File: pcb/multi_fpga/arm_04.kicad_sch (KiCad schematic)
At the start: 16 parts, among them U33 IM72D128V01XTMA1, U34 IM72D128V01XTMA1, U35 IM72D128V01XTMA1, U36 IM72D128V01XTMA1, U37 IM72D128V01XTMA1, U38 IM72D128V01XTMA1, U39 IM72D128V01XTMA1, U40 IM72D128V01XTMA1

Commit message: Fixed library and power issues.
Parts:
- C33, C34, C35, C36, C37, C38, C39, C40: symbol C -> multi_fpga:C
- U33, U34, U35, U36, U37, U38, U39, U40: symbol IM72D128 -> multi_fpga:IM72D128

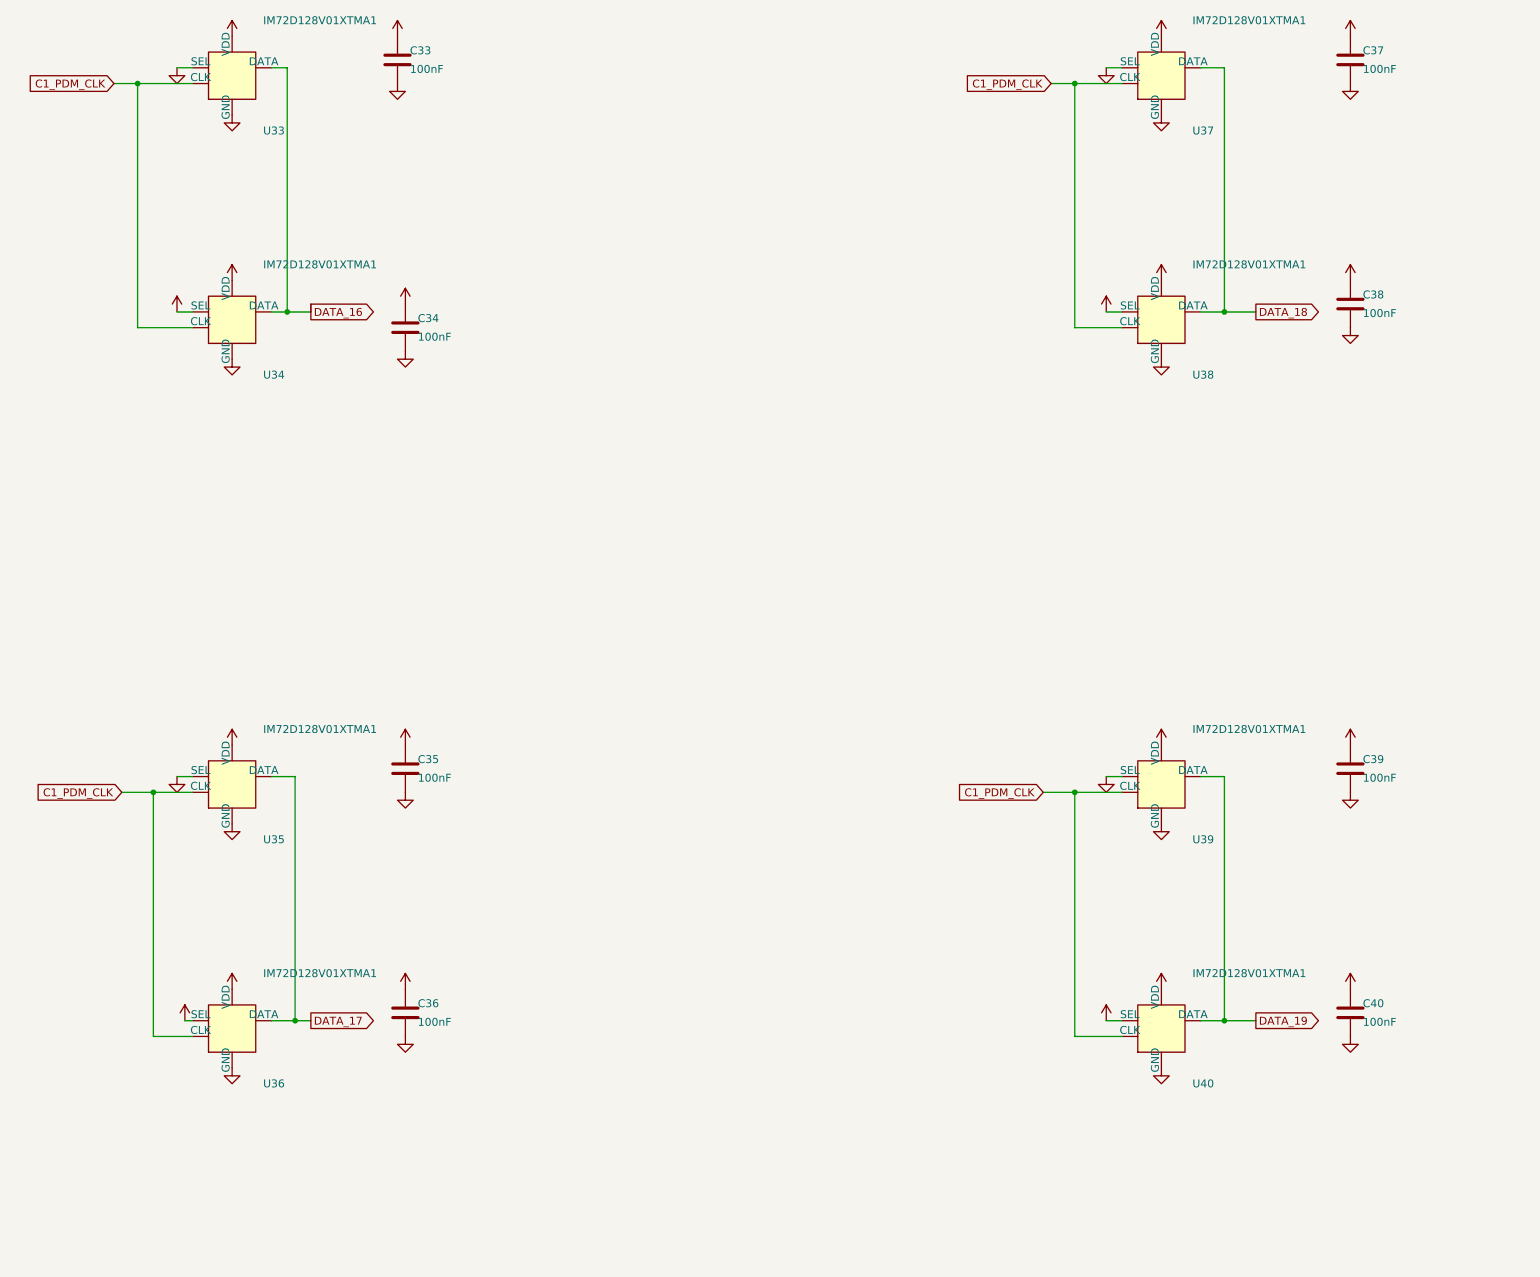
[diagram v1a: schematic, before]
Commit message: Fixed power and C ref des collisions.
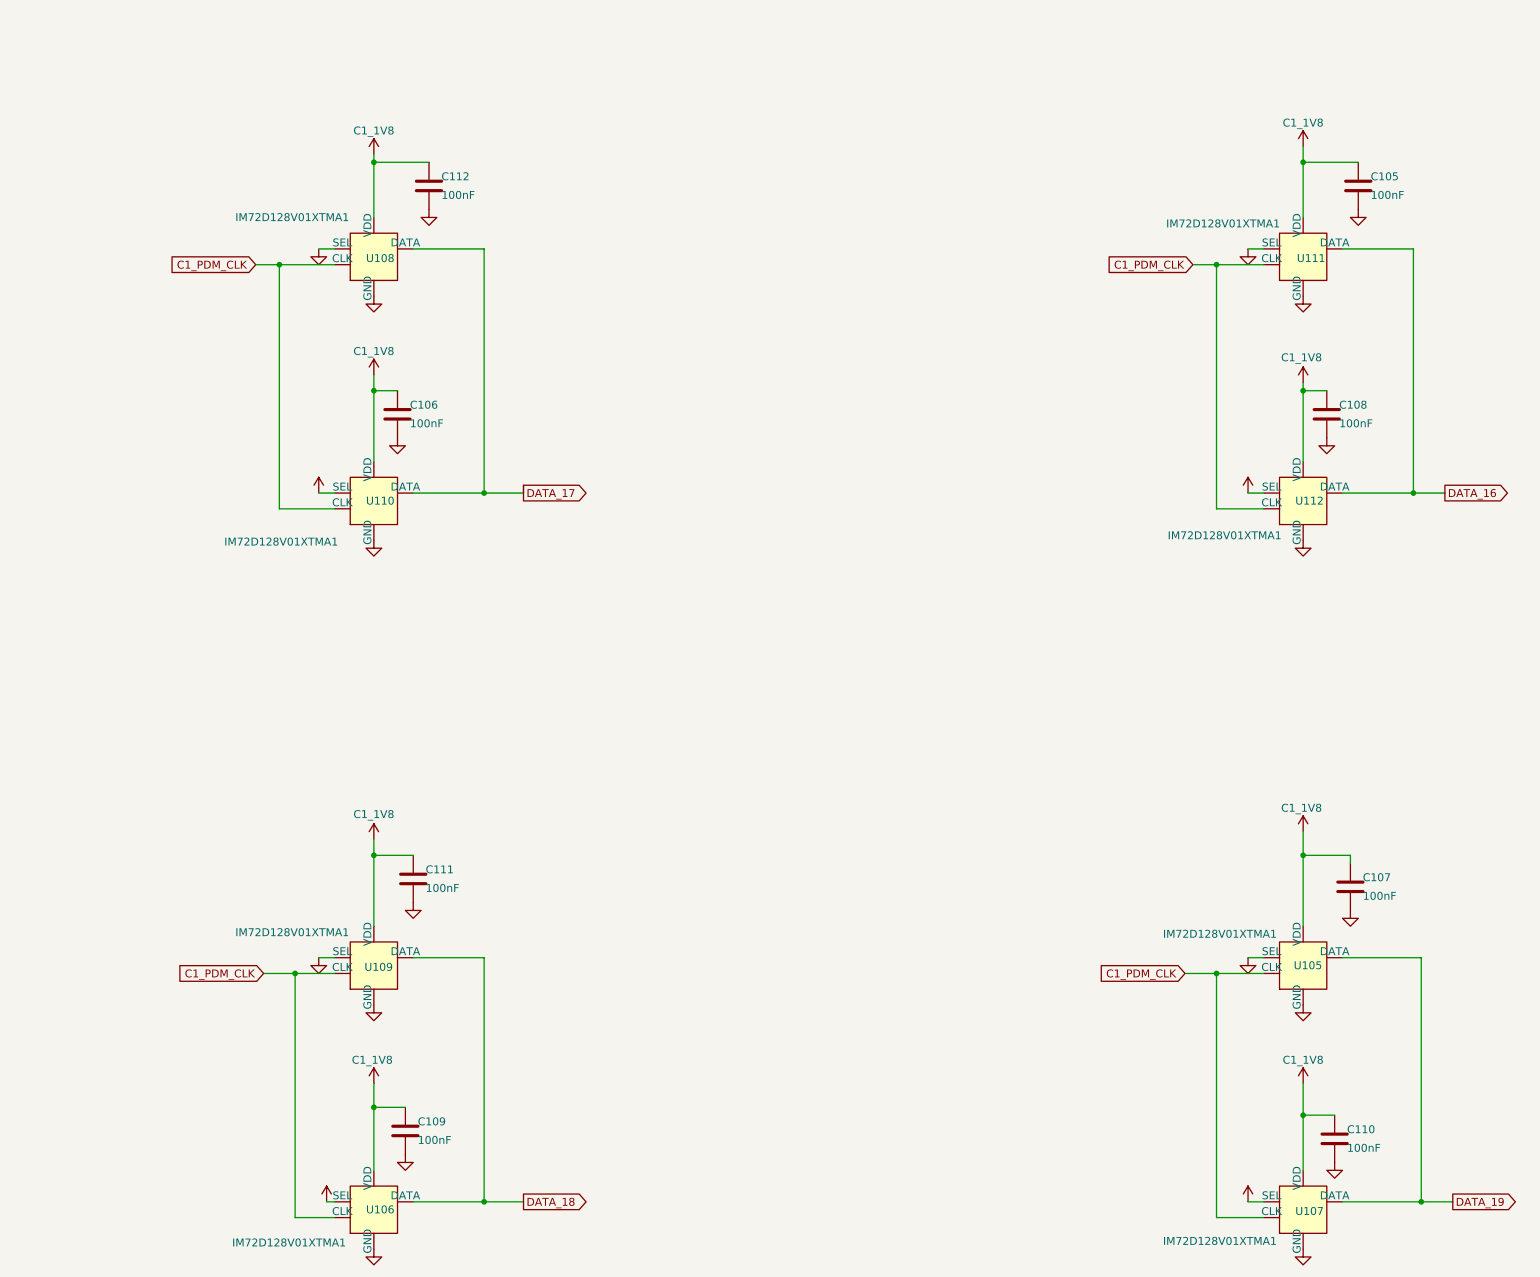
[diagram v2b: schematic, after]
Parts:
- removed C33, C34, C35, C36, C37, C38, C39, C40: 100nF, symbol multi_fpga:C
- removed U33, U34, U35, U36, U37, U38, U39, U40: IM72D128V01XTMA1, symbol multi_fpga:IM72D128
- added C105, C106, C107, C108, C109, C110, C111, C112: 100nF, symbol multi_fpga:C
- added U105, U106, U107, U108, U109, U110, U111, U112: IM72D128V01XTMA1, symbol multi_fpga:IM72D128
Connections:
- net C1_1V8: now also C105.1, C106.1, C107.1, C108.1, C109.1, C110.1, C111.1, C112.1, U105.2 (VDD), U106.2 (VDD), U106.4 (SEL), U107.2 (VDD), U107.4 (SEL), U108.2 (VDD), U109.2 (VDD), U110.2 (VDD), U110.4 (SEL), U111.2 (VDD), U112.2 (VDD), U112.4 (SEL)
- net C1_PDM_CLK: now also U105.3 (CLK), U106.3 (CLK), U107.3 (CLK), U108.3 (CLK), U109.3 (CLK), U110.3 (CLK), U111.3 (CLK), U112.3 (CLK)
- net DATA_16: now also U111.1 (DATA), U112.1 (DATA)
- net DATA_17: now also U108.1 (DATA), U110.1 (DATA)
- net DATA_18: now also U106.1 (DATA), U109.1 (DATA)
- net DATA_19: now also U105.1 (DATA), U107.1 (DATA)
- net GND: now also C105.2, C106.2, C107.2, C108.2, C109.2, C110.2, C111.2, C112.2, U105.4 (SEL), U105.5 (GND), U106.5 (GND), U107.5 (GND), U108.4 (SEL), U108.5 (GND), U109.4 (SEL), U109.5 (GND), U110.5 (GND), U111.4 (SEL), U111.5 (GND), U112.5 (GND)

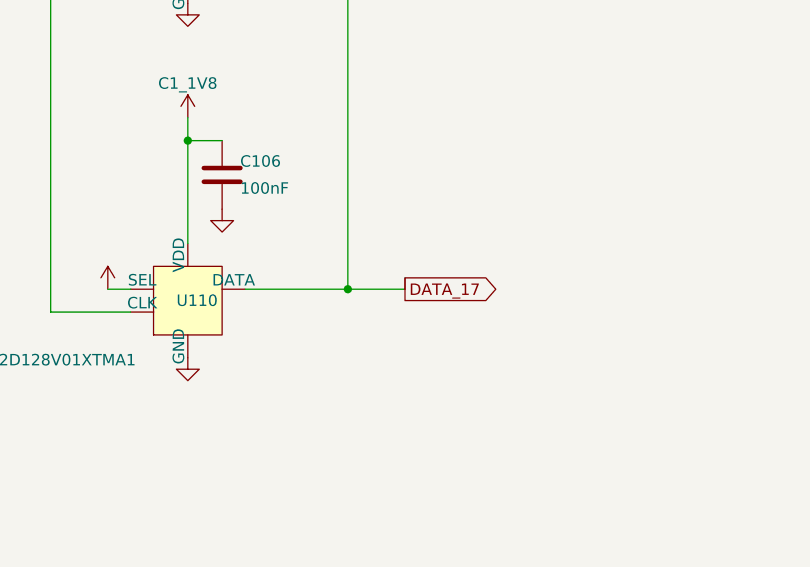
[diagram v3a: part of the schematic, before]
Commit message: Fixed regulator connection errors and dangling wire.
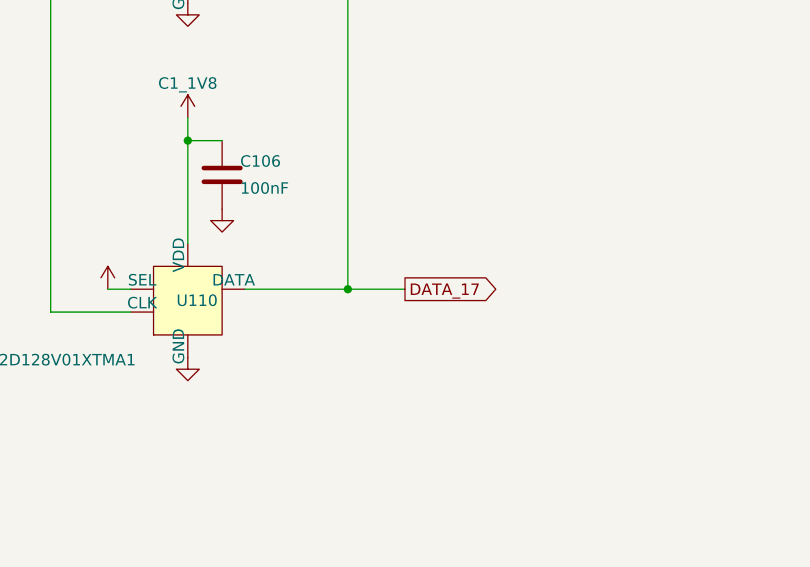
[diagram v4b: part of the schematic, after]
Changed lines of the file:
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@@
-	(wire
-		(pts
-			(xy 127 106.68) (xy 127 107.95)
-		)
-		(stroke
-			(width 0)
-			(type default)
-		)
-	)
 	(wire
 		(pts

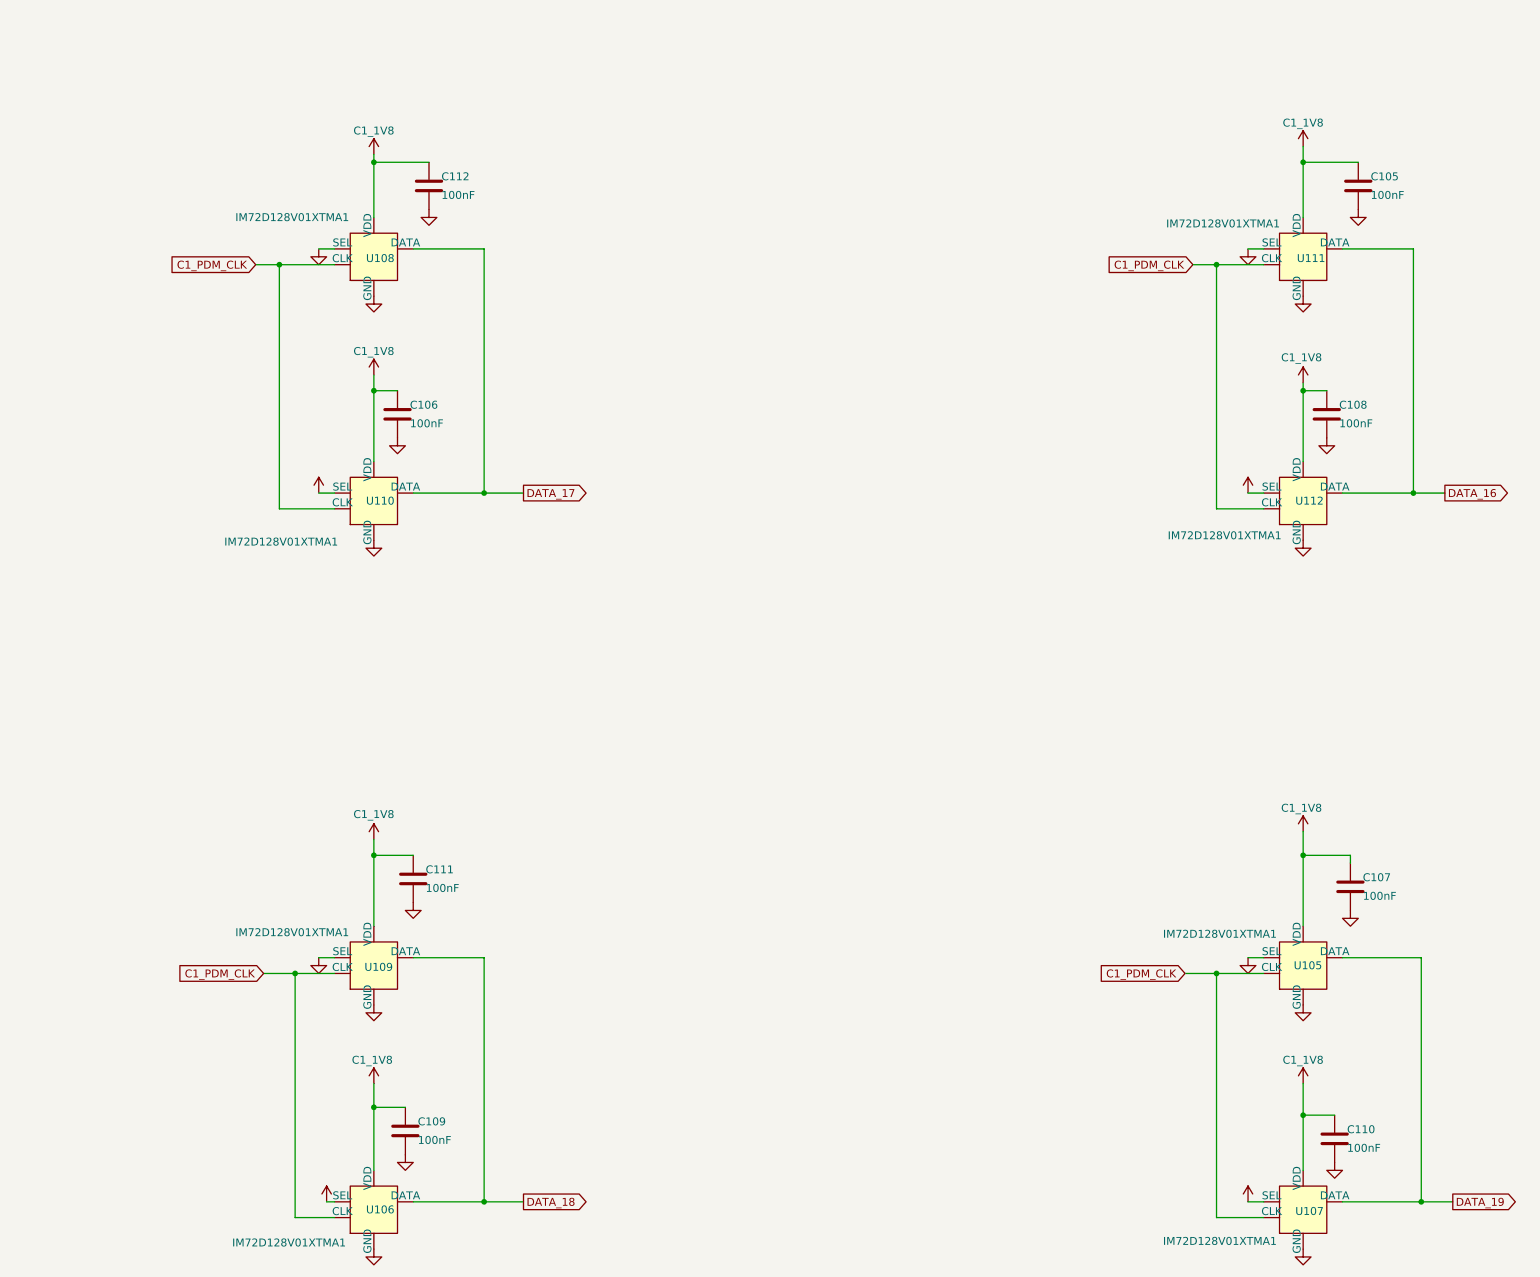
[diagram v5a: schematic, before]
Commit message: Global fix of res defs.
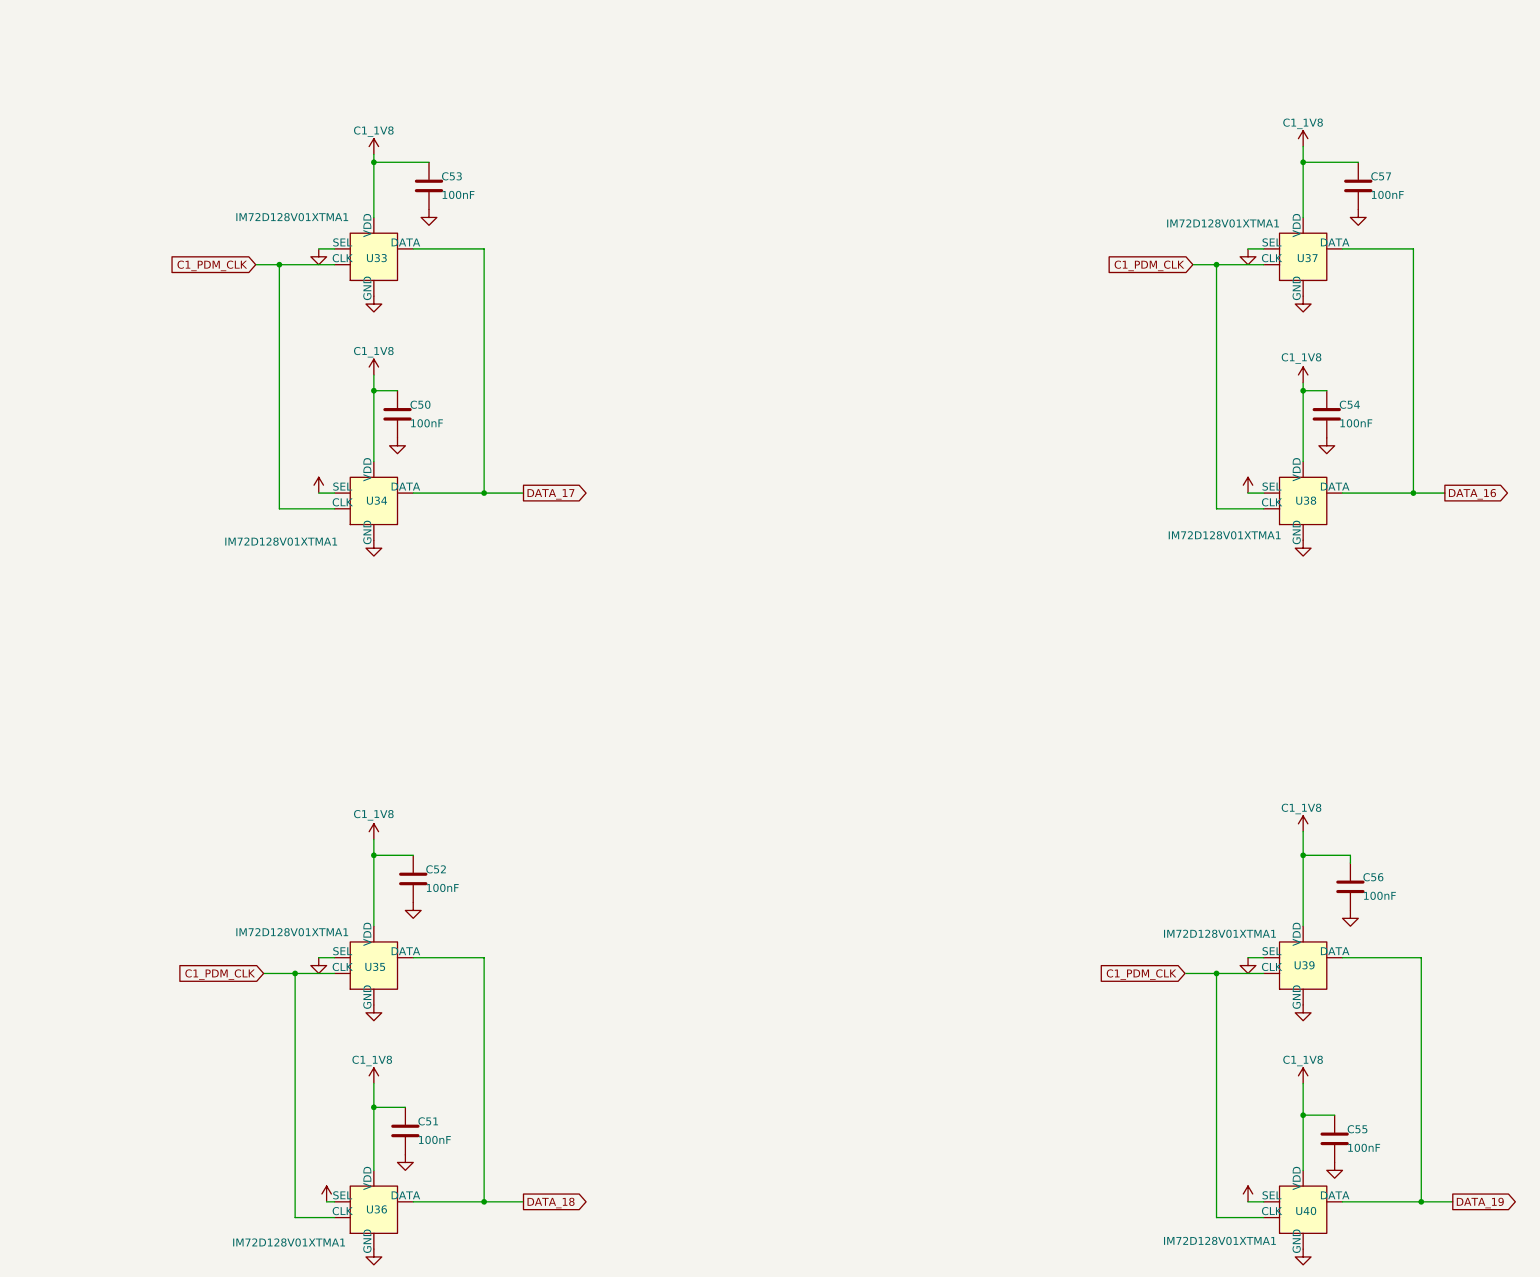
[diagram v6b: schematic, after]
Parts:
- renumbered C106 to C50, C109 to C51, C111 to C52, C112 to C53, C108 to C54, C110 to C55, C107 to C56, C105 to C57, U108 to U33, U110 to U34, U109 to U35, U106 to U36, U111 to U37, U112 to U38, U105 to U39, U107 to U40
